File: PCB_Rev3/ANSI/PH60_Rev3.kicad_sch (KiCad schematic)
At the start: 50 parts, among them J1 USB_C_Receptacle_USB2.0_16P, J2 Conn_01x02, J3 Conn_01x02_Pin, J4 Conn_01x02_Pin, J6 Conn_01x02_Pin, J8 Conn_01x02_Pin, SW1 SW_SPDT_321, U1 TLV62569DBV, U2 RP2040, U4 ETA6093, U6 W25Q16JVSS, Y1 Crystal_GND24

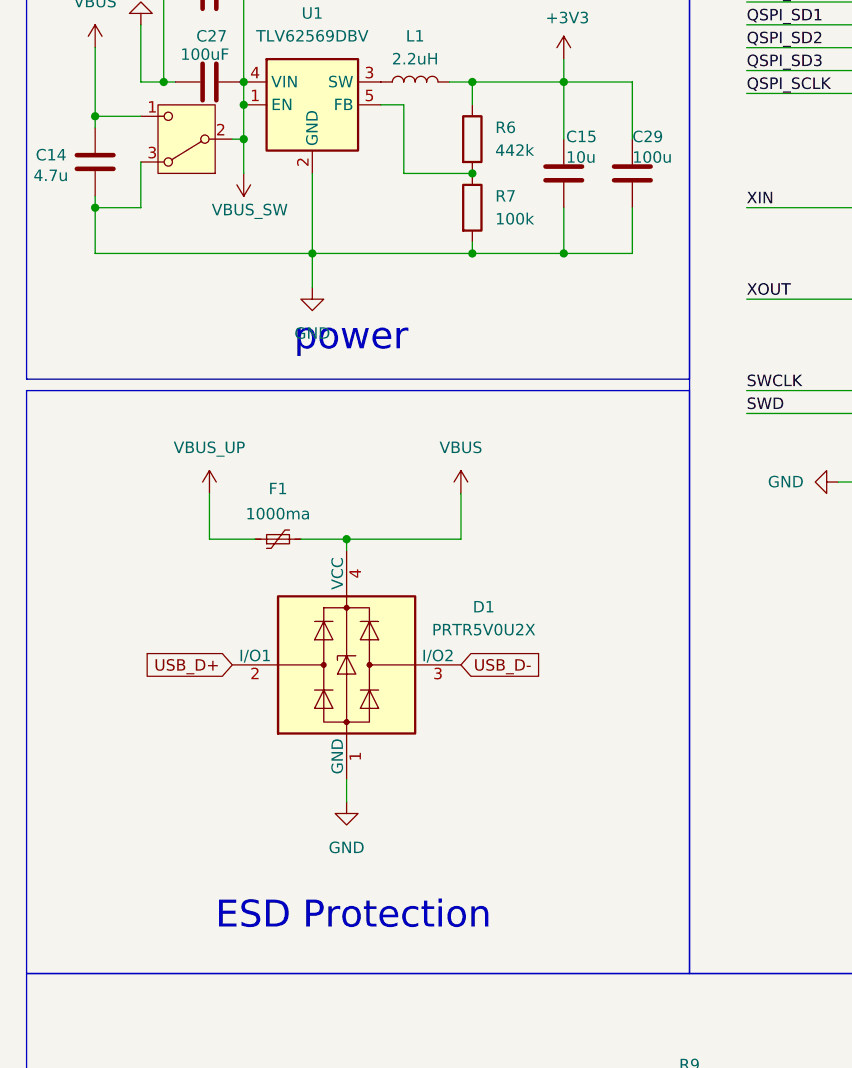
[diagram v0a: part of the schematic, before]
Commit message: 开关逻辑修改
取消开关接地，加入二极管以及mos管，注意：mos管封装引脚有修改
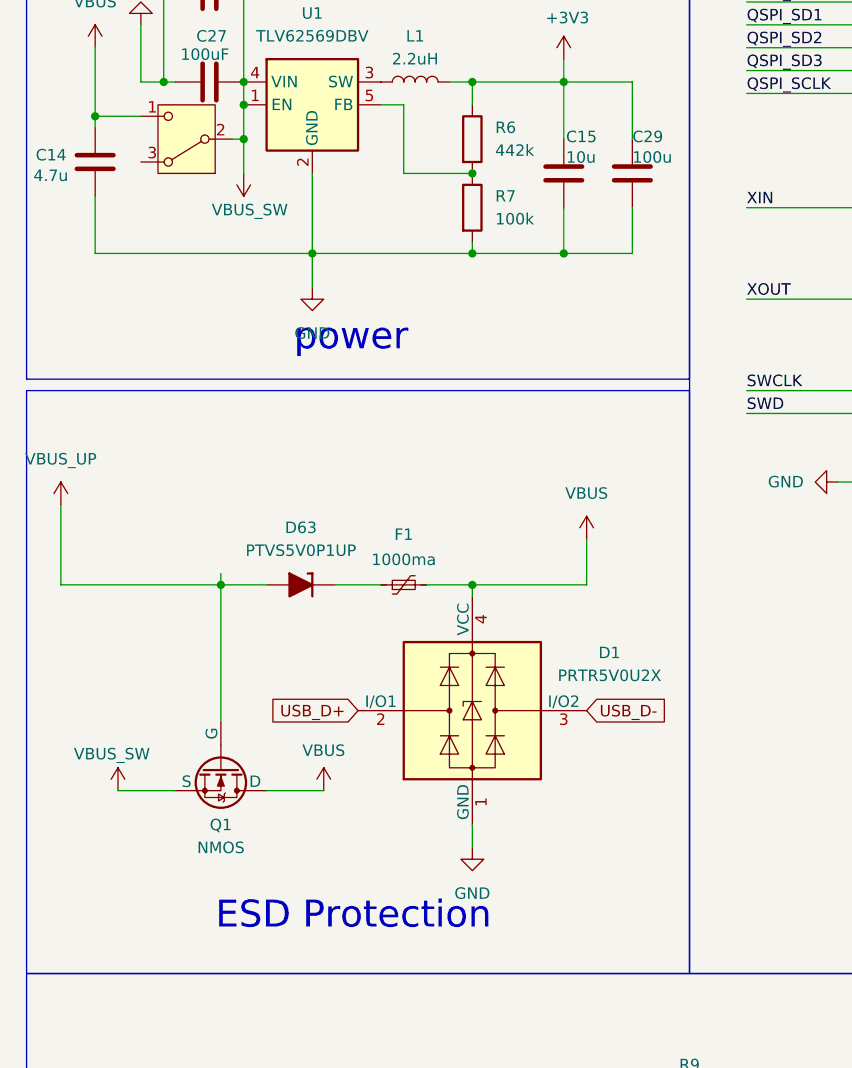
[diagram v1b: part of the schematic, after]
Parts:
- added D63: PTVS5V0P1UP, PCM_Diode_SMD_AKL:D_0603_1608Metric_TVS, symbol PCM_Diode_TVS_AKL:PTVS5V0P1UP
- added Q1: NMOS, Package_TO_SOT_SMD:SOT-23-3, symbol Simulation_SPICE:NMOS
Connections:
- net GND: no longer SW1.3 (A)
- net VBUS: now also Q1.1 (D)
- net VBUS_SW: now also Q1.3 (S)
- net VBUS_UP: now also D63.2 (A), Q1.2 (G); no longer F1.1
- new net: D63.1 (K), F1.1
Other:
- moved on the sheet: D1, F1

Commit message: REV3 与 REV3_A 合并
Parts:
- removed C17: 10u, Capacitor_SMD:C_0402_1005Metric, symbol Device:C
- removed C18: 22u, Capacitor_SMD:C_0402_1005Metric, symbol Device:C
- removed D63: PTVS5V0P1UP, PCM_Diode_SMD_AKL:D_0603_1608Metric_TVS, symbol PCM_Diode_TVS_AKL:PTVS5V0P1UP
- removed Q1: NMOS, Package_TO_SOT_SMD:SOT-23-3, symbol Simulation_SPICE:NMOS
- removed R11: 10k, PCM_Resistor_SMD_AKL:R_0402_1005Metric, symbol Device:R
- removed R9: 1k, PCM_Resistor_SMD_AKL:R_0402_1005Metric, symbol Device:R
- removed U4: ETA6093, Package_TO_SOT_SMD:SOT-23-5, symbol ETA6093:ETA6093
- added C20: 10u, Capacitor_SMD:C_0402_1005Metric, symbol Device:C
- added C21: 20u, Capacitor_SMD:C_0402_1005Metric, symbol Device:C
- added D2: PTVS5V0P1UP, PCM_Diode_SMD_AKL:D_SOD-882_DFN1006-2, symbol PCM_Diode_TVS_AKL:PTVS5V0P1UP
- added R10, R12, R13, R14, R15: 10k, PCM_Resistor_SMD_AKL:R_0402_1005Metric, symbol Device:R
- added TH1: 10k_NTC, PCM_4ms_Resistor:R_0603, symbol Device:Thermistor_NTC
- added U4: LGS5500EP, Package_SO:SOIC-8-1EP_3.9x4.9mm_P1.27mm_EP2.41x3.3mm, symbol Battery_Management:LGS5500EP
- BT1: footprint PH60:Molex_PicoBlade_With_Via -> Connector_Molex:Molex_PicoBlade_53261-0271_1x02-1MP_P1.25mm_Horizontal
- renumbered C28 to C13, C13 to C14, C27 to C15, C14 to C16, C15 to C17, C29 to C18, C16 to C19, J8 to J3, J3 to J4, J6 to J5, J4 to J6, R12 to R11, R10 to R9, U6 to U3
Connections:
- net +BATT: now also L2.2, C21.1, U4.3 (VL); no longer L2.1
- net CHRG: now also R15.1
- net GND: now also C20.2, C21.2, R10.2, R14.1, U4.9 (GND)
- net VBUS: now also C13.2, C15.2, U1.1 (EN), U1.4 (VIN), D2.1 (K); no longer D1.4 (VCC), F1.2
- net VBUS_UP: now also F1.1
- removed net VBUS_SW: C13.2, C15.2, SW1.2 (B), U1.1 (EN), U1.4 (VIN)
- new net: R12.2, R13.1, TH1.1
- new net: R13.2, TH1.2, U4.8 (NTC)
- new net: L2.1, U4.4 (LX)
- new net: SW1.2 (B), U4.5 (VH)
- new net: R15.2, U4.7 (VSET/LED)
- new net: R14.2, U4.1 (ISET)
- new net VBUS_in: C20.1, D1.4 (VCC), D2.2 (A), F1.2, R10.1, R12.1, U4.2 (VIN)
